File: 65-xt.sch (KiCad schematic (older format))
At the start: 177 parts, among them J1 Conn_01x04, Q1 2N7002, SW1 SW_Push, U1 MCP1700-3302E_SOT23, U2 STM32F072CBTx

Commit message: place components and route
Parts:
- MX39: footprint MX_Only:MXOnly-1.25U -> MX_Only:MXOnly-1.25U-FLIPPED
- U2: value STM32F072CBTx -> STM32F072CBT6
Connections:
- net CapsLED: now also U2.25 (PB12)
- net Col0: now also U2.45 (PB8)
- net Col1: now also U2.41 (PB5)
- net Col10: now also U2.20 (PB2)
- net Col11: now also U2.19 (PB1)
- net Col12: now also U2.18 (PB0)
- net Col13: now also U2.17 (PA7)
- net Col14: now also U2.16 (PA6)
- net Col15: now also U2.15 (PA5)
- net Col16: now also U2.14 (PA4)
- net Col17: now also U2.13 (PA3)
- net Col2: now also U2.12 (PA2)
- net Col3: now also U2.11 (PA1)
- net Col4: now also U2.10 (PA0)
- net Col5: now also MX74.1 (COL), U2.28 (PB15)
- net Col6: now also U2.27 (PB14)
- net Col7: now also U2.26 (PB13)
- net Col8: now also U2.22 (PB11)
- net Col9: now also U2.21 (PB10)
- net Row0: now also U2.42 (PB6)
- net Row1: now also U2.46 (PB9)
- net Row2: now also U2.31 (PA10)
- net Row3: now also U2.29 (PA8)
- net Row4: now also U2.30 (PA9)
- no-connect marks 3 -> 5
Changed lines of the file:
@@
 P 18950 5550
 F 0 "U2" H 18300 4050 50  0000 C CNN
-F 1 "STM32F072CBTx" H 18350 3950 50  0000 C CNN
+F 1 "STM32F072CBT6" H 18350 3950 50  0000 C CNN
 F 2 "Package_QFP:LQFP-48_7x7mm_P0.5mm" H 18350 4150 50  0001 R CNN
 F 3 "http://www.st.com/st-web-ui/static/active/en/resource/technical/document/datasheet/DM00090510.pdf" H 18950 5550 50  0001 C CNN
@@
 F 0 "MX39" H 9182 13824 60  0000 C CNN
 F 1 "MX-LED" H 9182 13750 20  0000 C CNN
-F 2 "MX_Only:MXOnly-1.25U" H 8475 13575 60  0001 C CNN
+F 2 "MX_Only:MXOnly-1.25U-FLIPPED" H 8475 13575 60  0001 C CNN
 F 3 "" H 8475 13575 60  0001 C CNN
 	1    9100 13600
@@
 Wire Wire Line
 	9450 13300 9750 13300
+Wire Wire Line
+	13250 16550 13500 16550
+Wire Wire Line
+	13500 16550 13500 15050
+Connection ~ 13500 15050
+Text GLabel 19550 5750 2    50   Input ~ 0
+Col16
+Text GLabel 19550 5650 2    50   Input ~ 0
+Col17
+Text GLabel 19550 5850 2    50   Input ~ 0
+Col15
+Text GLabel 19550 6050 2    50   Input ~ 0
+Col13
+Text GLabel 19550 5950 2    50   Input ~ 0
+Col14
+Text GLabel 18250 5350 0    50   Input ~ 0
+Col12
+Text GLabel 18250 5450 0    50   Input ~ 0
+Col11
+Text GLabel 18250 5550 0    50   Input ~ 0
+Col10
+Text GLabel 18250 6350 0    50   Input ~ 0
+Col9
+Text GLabel 18250 6450 0    50   Input ~ 0
+Col8
+Text GLabel 18250 6250 0    50   Input ~ 0
+Row1
+Text GLabel 18250 6150 0    50   Input ~ 0
+Col0
+NoConn ~ 19550 6650
+NoConn ~ 19550 6750
+Text GLabel 18250 6650 0    50   Input ~ 0
+Col7
+Text GLabel 18250 6750 0    50   Input ~ 0
+Col6
+Text GLabel 18250 6850 0    50   Input ~ 0
+Col5
+Text GLabel 19550 5350 2    50   Input ~ 0
+Col4
+Text GLabel 18250 5850 0    50   Input ~ 0
+Col1
+Text GLabel 19550 5550 2    50   Input ~ 0
+Col2
+Text GLabel 19550 5450 2    50   Input ~ 0
+Col3
+Text GLabel 19550 6150 2    50   Input ~ 0
+Row3
+Text GLabel 19550 6250 2    50   Input ~ 0
+Row4
+Text GLabel 18250 5950 0    50   Input ~ 0
+Row0
+Text GLabel 19550 6350 2    50   Input ~ 0
+Row2
+Text GLabel 18250 6550 0    50   Input ~ 0
+CapsLED
 $EndSCHEMATC

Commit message: remove submodule, update footprints
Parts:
- SW1: footprint acheron_Hardware:K2-1187SQ-A4SW-06 -> random-keyboard-parts:SKQG-1155865
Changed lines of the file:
@@
 F 0 "SW1" V 14696 2902 50  0000 R CNN
 F 1 "SW_Push" V 14605 2902 50  0000 R CNN
-F 2 "acheron_Hardware:K2-1187SQ-A4SW-06" H 14650 3150 50  0001 C CNN
+F 2 "random-keyboard-parts:SKQG-1155865" H 14650 3150 50  0001 C CNN
 F 3 "~" H 14650 3150 50  0001 C CNN
 	1    14650 2950

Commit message: moving things around
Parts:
- SW1: footprint random-keyboard-parts:SKQG-1155865 -> footprints-and-logos:K2-1187SQ-A4SW-06
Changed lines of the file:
@@
 F 0 "SW1" V 14696 2902 50  0000 R CNN
 F 1 "SW_Push" V 14605 2902 50  0000 R CNN
-F 2 "random-keyboard-parts:SKQG-1155865" H 14650 3150 50  0001 C CNN
+F 2 "footprints-and-logos:K2-1187SQ-A4SW-06" H 14650 3150 50  0001 C CNN
 F 3 "~" H 14650 3150 50  0001 C CNN
 	1    14650 2950

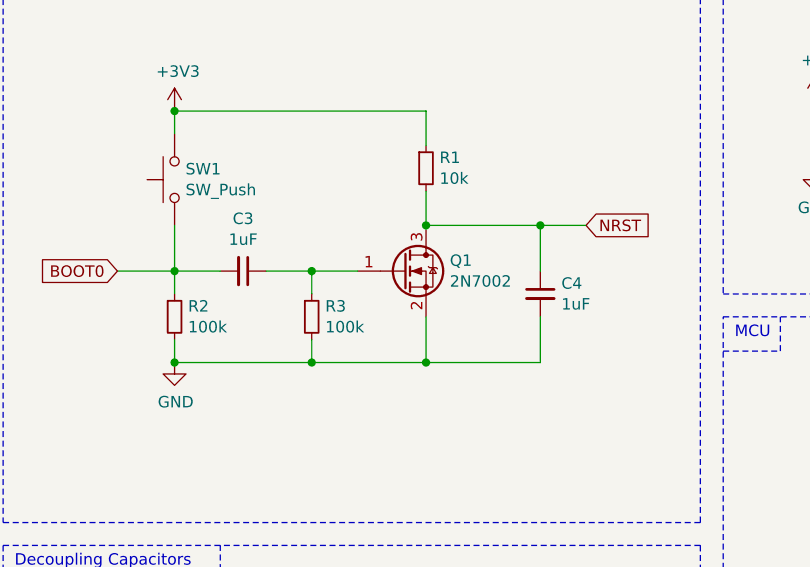
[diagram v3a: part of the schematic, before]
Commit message: updating reset/boot R and C values
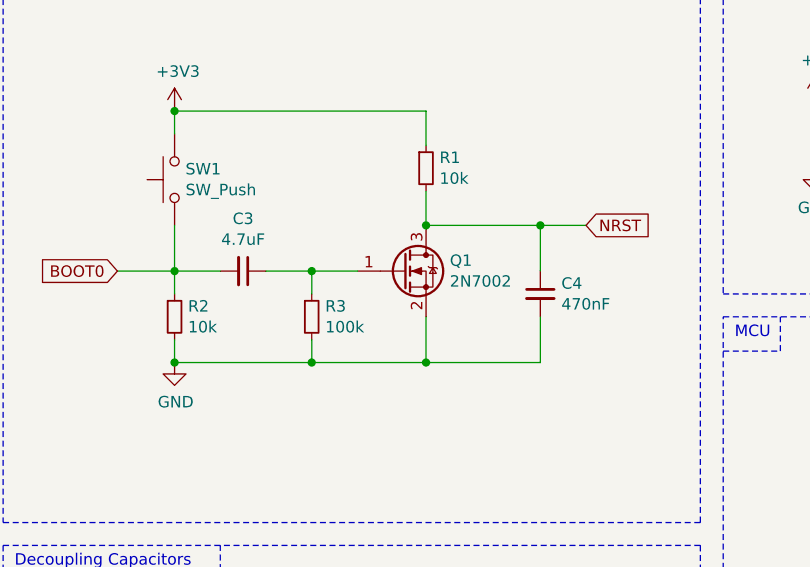
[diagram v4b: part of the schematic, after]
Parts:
- C3: value 1uF -> 4.7uF
- C4: value 1uF -> 470nF
- R2: value 100k -> 10k
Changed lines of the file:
@@
 P 14950 3350
 F 0 "C3" V 14721 3350 50  0000 C CNN
-F 1 "1uF" V 14812 3350 50  0000 C CNN
+F 1 "4.7uF" V 14812 3350 50  0000 C CNN
 F 2 "Capacitor_SMD:C_0603_1608Metric" H 14950 3350 50  0001 C CNN
 F 3 "~" H 14950 3350 50  0001 C CNN
@@
 P 14650 3550
 F 0 "R2" H 14709 3596 50  0000 L CNN
-F 1 "100k" H 14709 3505 50  0000 L CNN
+F 1 "10k" H 14709 3505 50  0000 L CNN
 F 2 "Resistor_SMD:R_0603_1608Metric" H 14650 3550 50  0001 C CNN
 F 3 "~" H 14650 3550 50  0001 C CNN
@@
 P 16250 3450
 F 0 "C4" H 16342 3496 50  0000 L CNN
-F 1 "1uF" H 16342 3405 50  0000 L CNN
+F 1 "470nF" H 16342 3405 50  0000 L CNN
 F 2 "Capacitor_SMD:C_0603_1608Metric" H 16250 3450 50  0001 C CNN
 F 3 "~" H 16250 3450 50  0001 C CNN
